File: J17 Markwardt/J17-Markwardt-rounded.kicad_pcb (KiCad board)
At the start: 2 copper layers, 16.5 x 28.8 mm, 6 parts, among them J1 USB_C_Receptacle_USB2.0, J2 829-22-005-20-001101

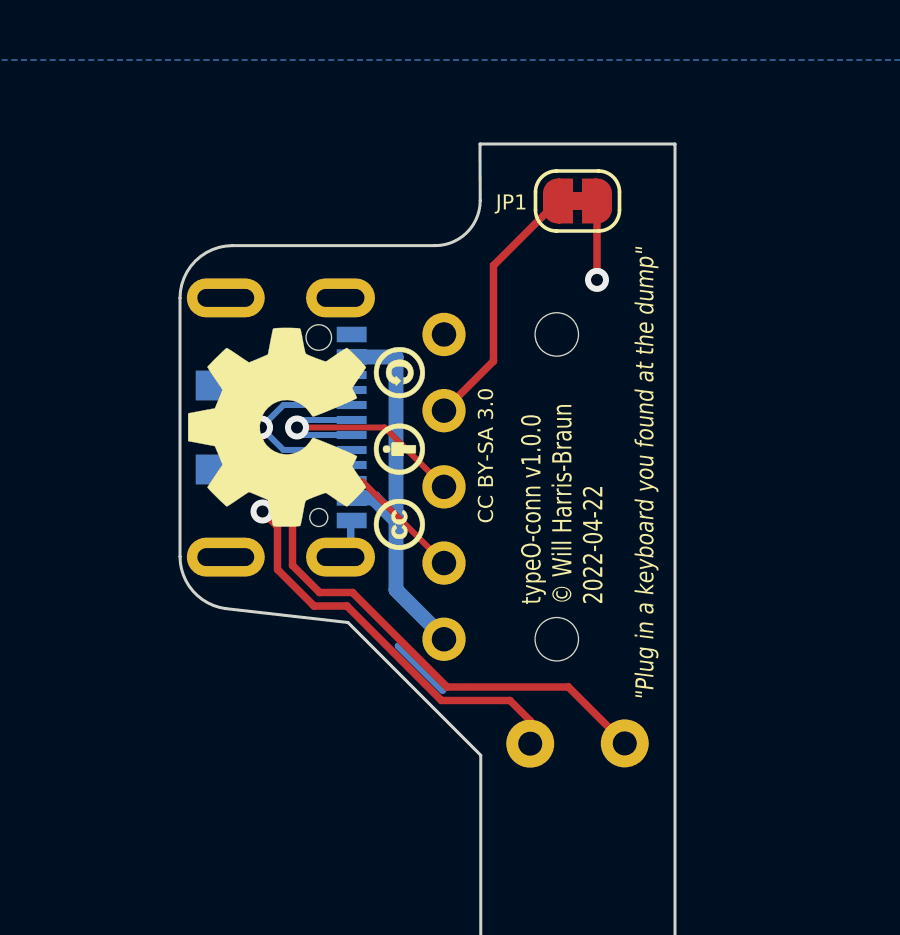
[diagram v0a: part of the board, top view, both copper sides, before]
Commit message: Rename connector to J17 Markwardt
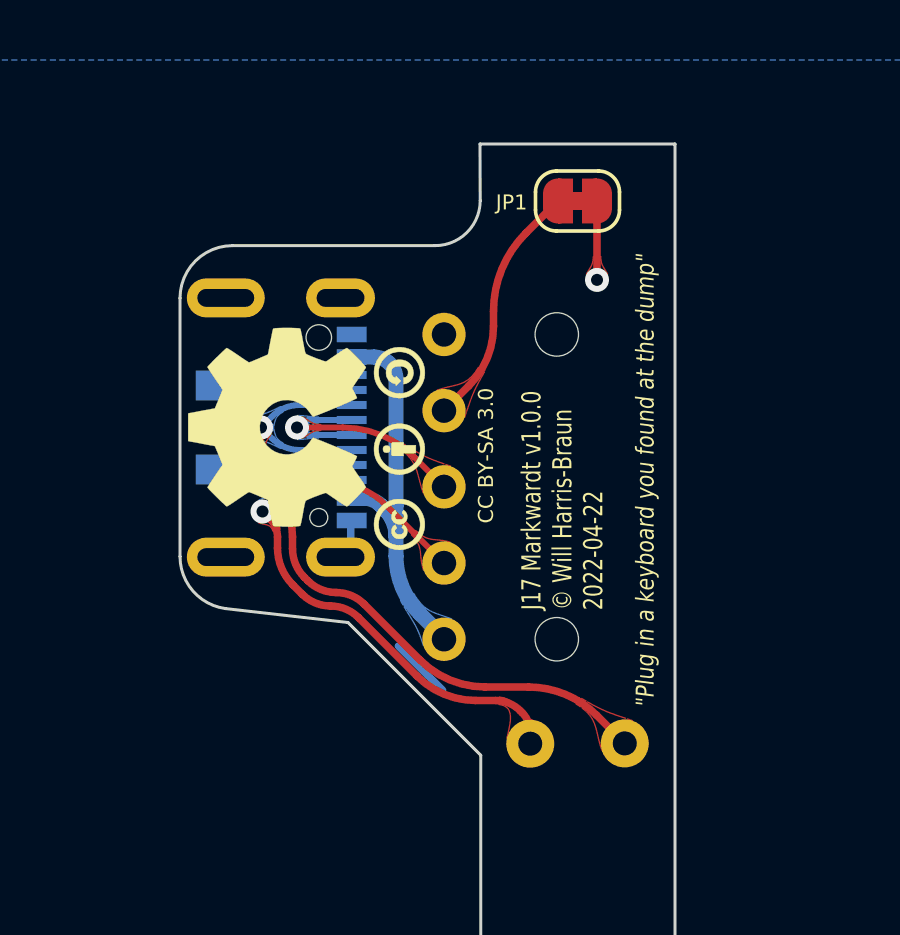
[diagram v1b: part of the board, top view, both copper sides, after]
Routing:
- net Net-(J1-PadB5): track 24.3 -> 23.4 mm
- net Net-(J1-PadA5): track 16.8 -> 16.3 mm
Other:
- board text added: "J17 Markwardt v1.0.0 © Will Harris-Braun 2022-04-22"
- board text removed: "typeO-conn v1.0.0 © Will Harris-Braun 2022-04-22"
